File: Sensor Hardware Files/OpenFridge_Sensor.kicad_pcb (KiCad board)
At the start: 2 copper layers, 2 parts, among them U1 TMP101, U2 STM32F103C8Tx

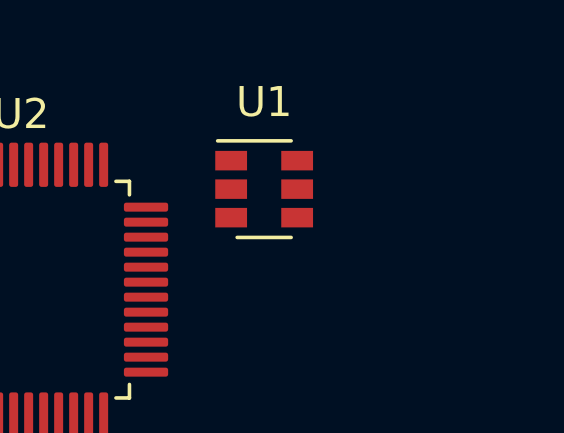
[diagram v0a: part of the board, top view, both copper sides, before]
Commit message: update bh17 footprint
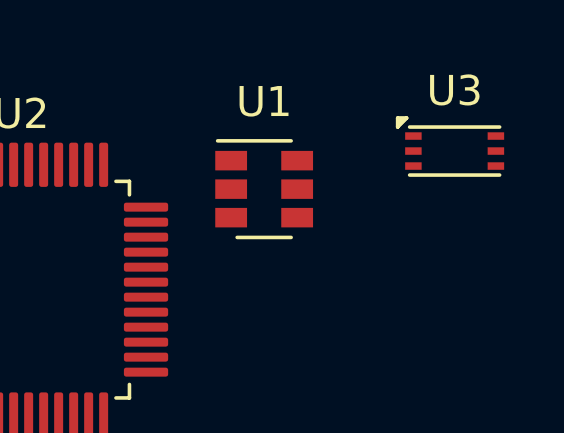
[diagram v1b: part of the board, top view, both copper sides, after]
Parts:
- added U3: BH1730FVC, OpenFridge_Sensor_Footprints:WSOF-6, F.Cu at (147.3, 86.4)

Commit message: update footprints
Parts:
- added U4: AT86RF231-ZU, Package_DFN_QFN:VQFN-32-1EP_5x5mm_P0.5mm_EP3.1x3.1mm, F.Cu at (142.2, 72.4)
- moved U3 24.7 mm to (127.0, 72.4)
- moved U1 24.4 mm to (121.9, 72.4)
- moved U2 9.26 mm to (127.0, 83.8)

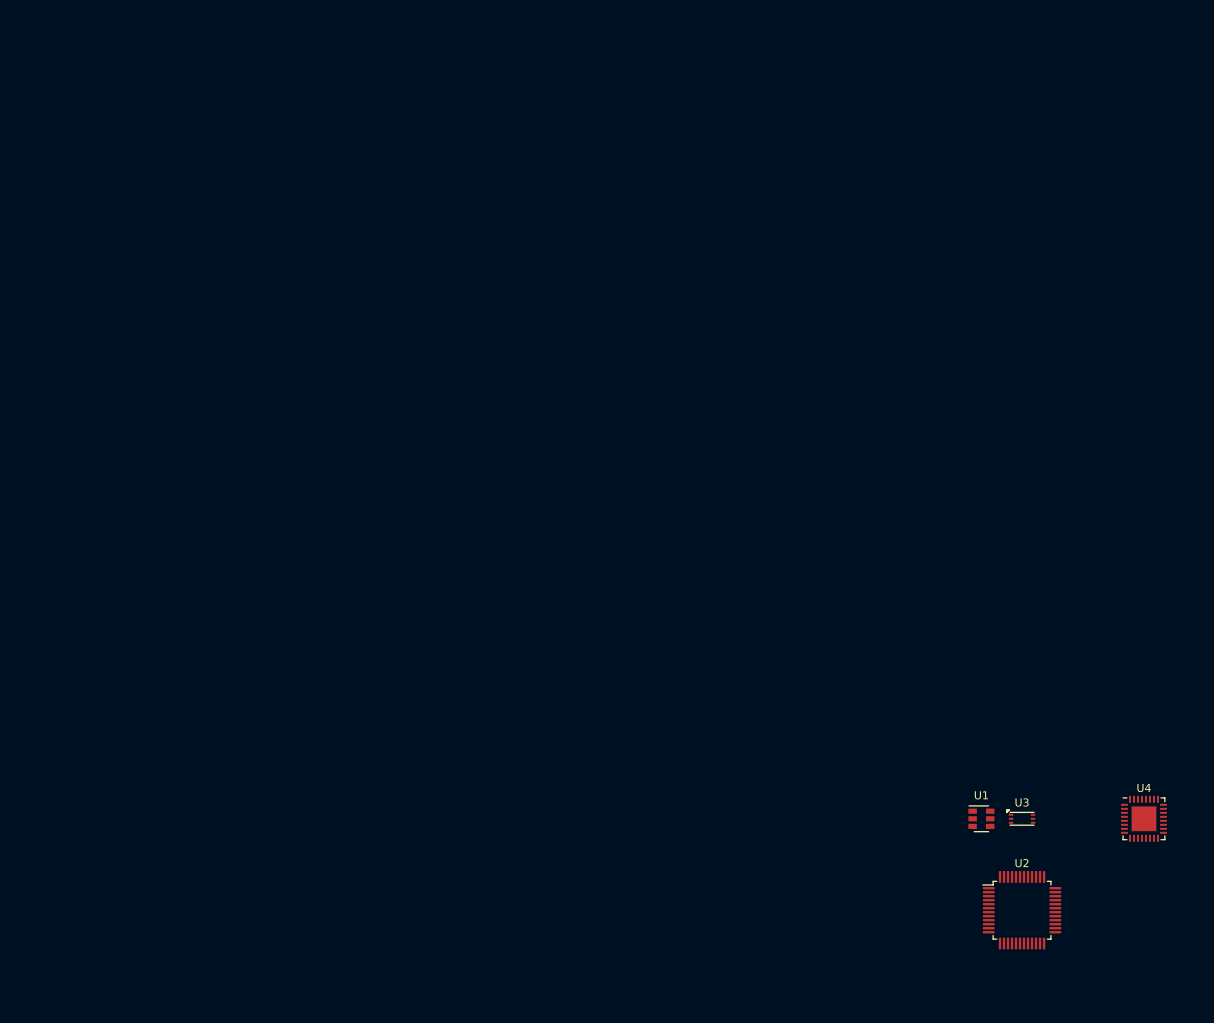
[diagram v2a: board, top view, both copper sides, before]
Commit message: add chip antenna and board outline
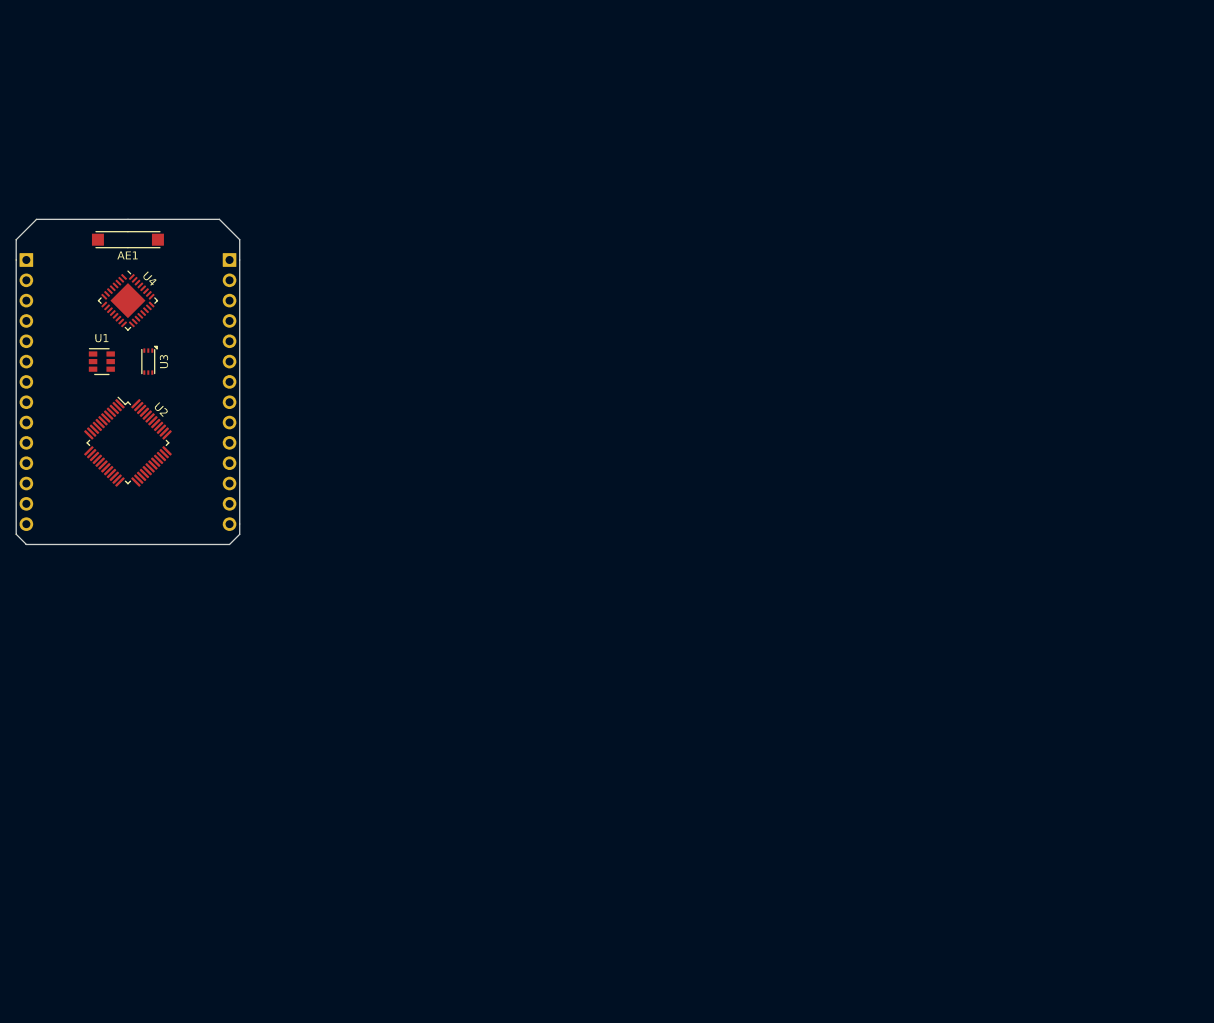
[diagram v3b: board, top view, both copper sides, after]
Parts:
- added AE1: Antenna_Chip, OpenFridge_Sensor_Footprints:RFANT8010080A3T, F.Cu at (15.2, 0.00)
- added J1: Conn_01x14, Connector_PinHeader_2.54mm:PinHeader_1x14_P2.54mm_Vertical, B.Cu at (27.9, 2.54)
- added J2: Conn_01x14, Connector_PinHeader_2.54mm:PinHeader_1x14_P2.54mm_Vertical, B.Cu at (2.54, 2.54)
- moved U4 142.6 mm to (15.2, 7.62), turned to 315 degrees
- moved U2 126.1 mm to (15.2, 25.4), turned to 315 degrees
- moved U1 123.9 mm to (12.0, 15.2)
- moved U3 123.3 mm to (17.8, 15.2), turned to 270 degrees
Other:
- board outline added: 27.9 x 40.6 mm

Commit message: update RF IC passives
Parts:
- added C1: C, Capacitor_SMD:C_0805_2012Metric_Pad1.18x1.45mm_HandSolder, F.Cu at (17.2, 6.40)
- added C2: C, Capacitor_SMD:C_0805_2012Metric_Pad1.18x1.45mm_HandSolder, F.Cu at (13.8, 5.25)
- added C3: C, Capacitor_SMD:C_0805_2012Metric_Pad1.18x1.45mm_HandSolder, F.Cu at (17.2, 4.20)
- added C4: 12pF, Capacitor_SMD:C_0805_2012Metric_Pad1.18x1.45mm_HandSolder, F.Cu at (79.6, -25.2)
- added C5: 12pF, Capacitor_SMD:C_0805_2012Metric_Pad1.18x1.45mm_HandSolder, F.Cu at (79.6, -22.2)
- added R1: R, Resistor_SMD:R_0805_2012Metric_Pad1.20x1.40mm_HandSolder, F.Cu at (11.5, 3.25)
- added Y1: 16 MHz 12pF, Crystal:Crystal_SMD_3225-4Pin_3.2x2.5mm_HandSoldering, F.Cu at (73.8, -23.9)
- U4: value AT86RF231-ZU -> XN297LBW; footprint Package_DFN_QFN:VQFN-32-1EP_5x5mm_P0.5mm_EP3.1x3.1mm -> Package_SO:SOP-8_3.9x4.9mm_P1.27mm
- moved U3 24.5 mm to (12.0, -8.60)
- moved U1 24.4 mm to (8.00, -8.80)
- moved U4 4.60 mm to (14.8, 12.2), turned to 90 degrees
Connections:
- AE1 pad 1: Net-(AE1-Pad1) -> GND
- U4 pad 7: Net-(U4-Pad7) -> GND
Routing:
- net Net-(C1-Pad2): track 0.00 -> 6.10 mm
- net Net-(C2-Pad1): track 0.00 -> 4.55 mm
- net Net-(AE1-Pad2): track 0.00 -> 2.25 mm

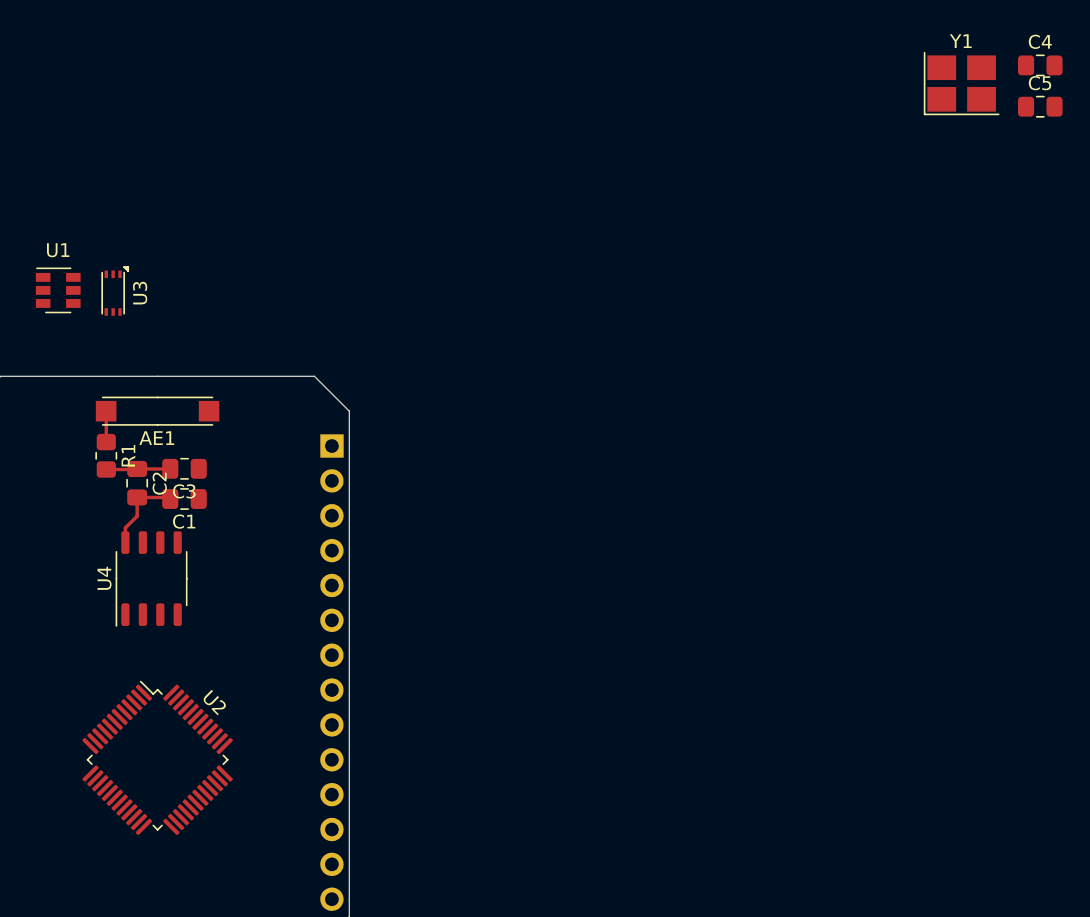
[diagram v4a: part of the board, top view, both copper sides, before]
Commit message: update rf passives
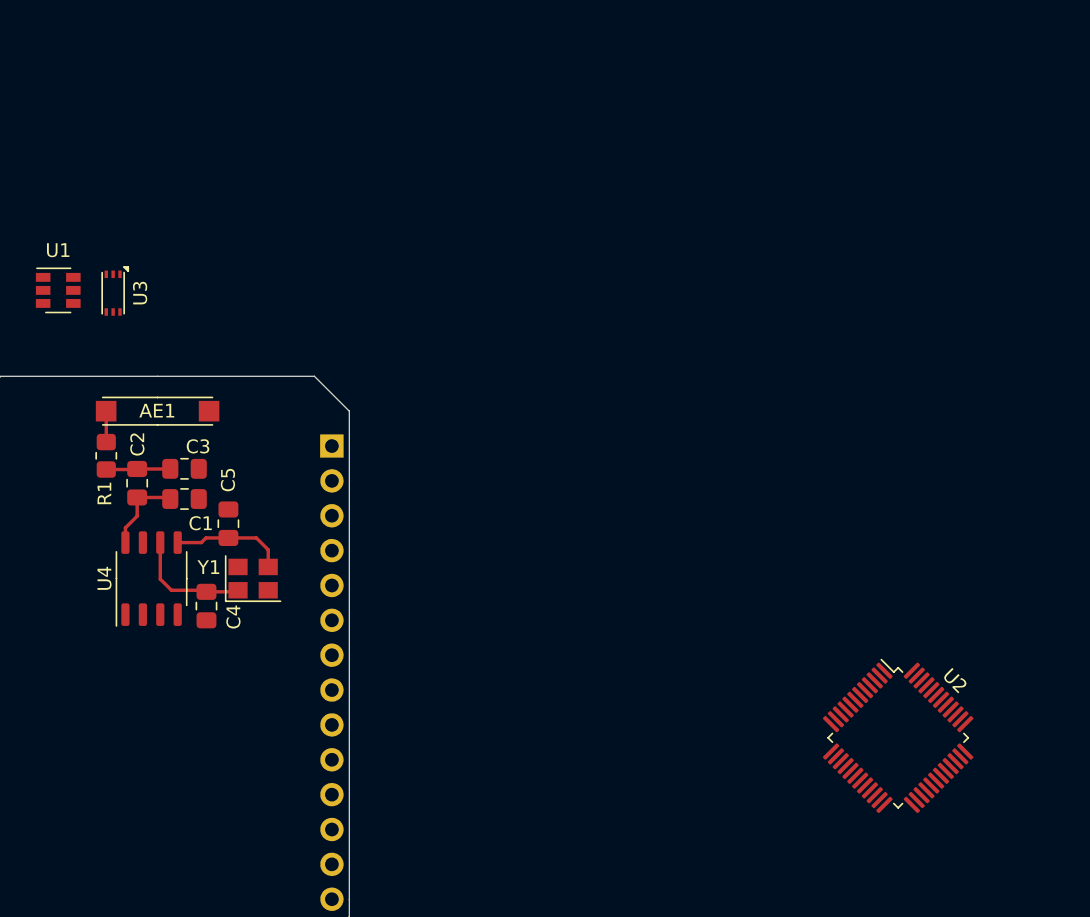
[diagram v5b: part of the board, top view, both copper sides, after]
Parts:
- Y1: footprint Crystal:Crystal_SMD_3225-4Pin_3.2x2.5mm_HandSoldering -> Crystal:Crystal_SMD_3225-4Pin_3.2x2.5mm
- moved C4 72.4 mm to (18.8, 14.2), turned to 90 degrees
- moved C5 66.5 mm to (20.4, 8.20), turned to 270 degrees
- moved Y1 63.0 mm to (22.2, 12.2)
- moved U2 54.0 mm to (69.2, 23.8)
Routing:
- net Net-(C4-Pad2): track 0.00 -> 8.81 mm
- net Net-(C5-Pad2): track 0.00 -> 8.34 mm
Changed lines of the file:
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@@
     (thickness 1.6)
     (drawings 176)
-    (tracks 11)
+    (tracks 22)
     (zones 0)
     (modules 14)
@@
     (40 Dwgs.User user)
     (41 Cmts.User user)
-    (42 Eco1.User user)
+    (42 Eco1.User user hide)
     (43 Eco2.User user)
     (44 Edge.Cuts user)
@@
     (add_net "Net-(U4-Pad4)")
   )
-  (module Crystal:Crystal_SMD_3225-4Pin_3.2x2.5mm_HandSoldering (layer F.Cu)
-    (at 73.825001 -23.874999)
-    (descr "SMD Crystal SERIES SMD3225/4 http://www.txccrystal.com/images/pdf/7m-accuracy.pdf, hand-soldering, 3.2x2.5mm^2 package")
-    (tags "SMD SMT crystal hand-soldering")
+  (module Crystal:Crystal_SMD_3225-4Pin_3.2x2.5mm (layer F.Cu)
+    (at 22.2 12.2)
+    (descr "SMD Crystal SERIES SMD3225/4 http://www.txccrystal.com/images/pdf/7m-accuracy.pdf, 3.2x2.5mm^2 package")
+    (tags "SMD SMT crystal")
     (attr smd)
-    (fp_text reference Y1 (at 0 -3.05) (layer F.SilkS)
-      (effects (font (size 1 1) (thickness 0.15)))
-    )
-    (fp_text value "16 MHz 12pF" (at 0 3.05) (layer F.Fab)
+    (fp_text reference Y1 (at -3.2 -0.8) (layer F.SilkS)
+      (effects (font (size 1 1) (thickness 0.15)))
+    )
+    (fp_text value "16 MHz 12pF" (at 0 2.45) (layer F.Fab)
       (effects (font (size 1 1) (thickness 0.15)))
     )
@@
     (fp_line (start 1.6 -1.25) (end -1.6 -1.25) (layer F.Fab) (width 0.1))
     (fp_line (start -1.6 0.25) (end -0.6 1.25) (layer F.Fab) (width 0.1))
-    (fp_line (start -2.7 -2.25) (end -2.7 2.25) (layer F.SilkS) (width 0.12))
-    (fp_line (start -2.7 2.25) (end 2.7 2.25) (layer F.SilkS) (width 0.12))
-    (fp_line (start -2.8 -2.3) (end -2.8 2.3) (layer F.CrtYd) (width 0.05))
-    (fp_line (start -2.8 2.3) (end 2.8 2.3) (layer F.CrtYd) (width 0.05))
-    (fp_line (start 2.8 2.3) (end 2.8 -2.3) (layer F.CrtYd) (width 0.05))
-    (fp_line (start 2.8 -2.3) (end -2.8 -2.3) (layer F.CrtYd) (width 0.05))
-    (pad 4 smd rect (at -1.45 -1.15) (size 2.1 1.8) (layers F.Cu F.Paste F.Mask)
+    (fp_line (start -2 -1.65) (end -2 1.65) (layer F.SilkS) (width 0.12))
+    (fp_line (start -2 1.65) (end 2 1.65) (layer F.SilkS) (width 0.12))
+    (fp_line (start -2.1 -1.7) (end -2.1 1.7) (layer F.CrtYd) (width 0.05))
+    (fp_line (start -2.1 1.7) (end 2.1 1.7) (layer F.CrtYd) (width 0.05))
+    (fp_line (start 2.1 1.7) (end 2.1 -1.7) (layer F.CrtYd) (width 0.05))
+    (fp_line (start 2.1 -1.7) (end -2.1 -1.7) (layer F.CrtYd) (width 0.05))
+    (pad 4 smd rect (at -1.1 -0.85) (size 1.4 1.2) (layers F.Cu F.Paste F.Mask)
       (net 92 GND))
-    (pad 3 smd rect (at 1.45 -1.15) (size 2.1 1.8) (layers F.Cu F.Paste F.Mask)
+    (pad 3 smd rect (at 1.1 -0.85) (size 1.4 1.2) (layers F.Cu F.Paste F.Mask)
       (net 96 "Net-(C5-Pad2)"))
-    (pad 2 smd rect (at 1.45 1.15) (size 2.1 1.8) (layers F.Cu F.Paste F.Mask)
+    (pad 2 smd rect (at 1.1 0.85) (size 1.4 1.2) (layers F.Cu F.Paste F.Mask)
       (net 92 GND))
-    (pad 1 smd rect (at -1.45 1.15) (size 2.1 1.8) (layers F.Cu F.Paste F.Mask)
+    (pad 1 smd rect (at -1.1 0.85) (size 1.4 1.2) (layers F.Cu F.Paste F.Mask)
       (net 95 "Net-(C4-Pad2)"))
-    (model ${KISYS3DMOD}/Crystal.3dshapes/Crystal_SMD_3225-4Pin_3.2x2.5mm_HandSoldering.wrl
+    (model ${KISYS3DMOD}/Crystal.3dshapes/Crystal_SMD_3225-4Pin_3.2x2.5mm.wrl
       (at (xyz 0 0 0))
       (scale (xyz 1 1 1))
@@
   )
   (module Capacitor_SMD:C_0805_2012Metric_Pad1.18x1.45mm_HandSolder (layer F.Cu)
-    (at 79.555001 -22.184999)
+    (at 20.4 8.2 270)
     (descr "Capacitor SMD 0805 (2012 Metric), square (rectangular) end terminal, IPC_7351 nominal with elongated pad for handsoldering. (Body size source: IPC-SM-782 page 76, https://www.pcb-3d.com/wordpress/wp-content/uploads/ipc-sm-782a_amendment_1_and_2.pdf, https://docs.google.com/spreadsheets/d/1BsfQQcO9C6DZCsRaXUlFlo91Tg2WpOkGARC1WS5S8t0/edit?usp=sharing), generated with kicad-footprint-generator")
     (tags "capacitor handsolder")
     (attr smd)
-    (fp_text reference C5 (at 0 -1.68) (layer F.SilkS)
-      (effects (font (size 1 1) (thickness 0.15)))
-    )
-    (fp_text value 12pF (at 0 1.68) (layer F.Fab)
-      (effects (font (size 1 1) (thickness 0.15)))
-    )
-    (fp_text user %R (at 0 0) (layer F.Fab)
+    (fp_text reference C5 (at -3.2 0 90) (layer F.SilkS)
+      (effects (font (size 1 1) (thickness 0.15)))
+    )
+    (fp_text value 12pF (at 0 1.68 90) (layer F.Fab)
+      (effects (font (size 1 1) (thickness 0.15)))
+    )
+    (fp_text user %R (at 0 0 90) (layer F.Fab)
       (effects (font (size 0.5 0.5) (thickness 0.08)))
     )
@@
     (fp_line (start 1.88 -0.98) (end 1.88 0.98) (layer F.CrtYd) (width 0.05))
     (fp_line (start 1.88 0.98) (end -1.88 0.98) (layer F.CrtYd) (width 0.05))
-    (pad 2 smd roundrect (at 1.0375 0) (size 1.175 1.45) (layers F.Cu F.Paste F.Mask) (roundrect_rratio 0.212766)
+    (pad 2 smd roundrect (at 1.0375 0 270) (size 1.175 1.45) (layers F.Cu F.Paste F.Mask) (roundrect_rratio 0.212766)
       (net 96 "Net-(C5-Pad2)"))
-    (pad 1 smd roundrect (at -1.0375 0) (size 1.175 1.45) (layers F.Cu F.Paste F.Mask) (roundrect_rratio 0.212766)
+    (pad 1 smd roundrect (at -1.0375 0 270) (size 1.175 1.45) (layers F.Cu F.Paste F.Mask) (roundrect_rratio 0.212766)
       (net 92 GND))
     (model ${KISYS3DMOD}/Capacitor_SMD.3dshapes/C_0805_2012Metric.wrl
@@
   )
   (module Capacitor_SMD:C_0805_2012Metric_Pad1.18x1.45mm_HandSolder (layer F.Cu)
-    (at 79.555001 -25.194999)
+    (at 18.8 14.2 90)
     (descr "Capacitor SMD 0805 (2012 Metric), square (rectangular) end terminal, IPC_7351 nominal with elongated pad for handsoldering. (Body size source: IPC-SM-782 page 76, https://www.pcb-3d.com/wordpress/wp-content/uploads/ipc-sm-782a_amendment_1_and_2.pdf, https://docs.google.com/spreadsheets/d/1BsfQQcO9C6DZCsRaXUlFlo91Tg2WpOkGARC1WS5S8t0/edit?usp=sharing), generated with kicad-footprint-generator")
     (tags "capacitor handsolder")
     (attr smd)
-    (fp_text reference C4 (at 0 -1.68) (layer F.SilkS)
-      (effects (font (size 1 1) (thickness 0.15)))
-    )
-    (fp_text value 12pF (at 0 1.68) (layer F.Fab)
-      (effects (font (size 1 1) (thickness 0.15)))
-    )
-    (fp_text user %R (at 0 0) (layer F.Fab)
+    (fp_text reference C4 (at -0.8 2 90) (layer F.SilkS)
+      (effects (font (size 1 1) (thickness 0.15)))
+    )
+    (fp_text value 12pF (at 0 1.68 90) (layer F.Fab)
+      (effects (font (size 1 1) (thickness 0.15)))
+    )
+    (fp_text user %R (at 0 0 90) (layer F.Fab)
       (effects (font (size 0.5 0.5) (thickness 0.08)))
     )
@@
     (fp_line (start 1.88 -0.98) (end 1.88 0.98) (layer F.CrtYd) (width 0.05))
     (fp_line (start 1.88 0.98) (end -1.88 0.98) (layer F.CrtYd) (width 0.05))
-    (pad 2 smd roundrect (at 1.0375 0) (size 1.175 1.45) (layers F.Cu F.Paste F.Mask) (roundrect_rratio 0.212766)
+    (pad 2 smd roundrect (at 1.0375 0 90) (size 1.175 1.45) (layers F.Cu F.Paste F.Mask) (roundrect_rratio 0.212766)
       (net 95 "Net-(C4-Pad2)"))
-    (pad 1 smd roundrect (at -1.0375 0) (size 1.175 1.45) (layers F.Cu F.Paste F.Mask) (roundrect_rratio 0.212766)
+    (pad 1 smd roundrect (at -1.0375 0 90) (size 1.175 1.45) (layers F.Cu F.Paste F.Mask) (roundrect_rratio 0.212766)
       (net 92 GND))
     (model ${KISYS3DMOD}/Capacitor_SMD.3dshapes/C_0805_2012Metric.wrl
@@
     (tags "resistor handsolder")
     (attr smd)
-    (fp_text reference R1 (at 0 -1.65 90) (layer F.SilkS)
+    (fp_text reference R1 (at 2.75 0.1 90) (layer F.SilkS)
       (effects (font (size 1 1) (thickness 0.15)))
     )
@@
     (tags "capacitor handsolder")
     (attr smd)
-    (fp_text reference C3 (at 0 -1.68) (layer F.SilkS)
+    (fp_text reference C3 (at -1 1.6) (layer F.SilkS)
       (effects (font (size 1 1) (thickness 0.15)))
     )
@@
     (tags "capacitor handsolder")
     (attr smd)
-    (fp_text reference C2 (at 0 -1.68 90) (layer F.SilkS)
+    (fp_text reference C2 (at -2.85 -0.05 90) (layer F.SilkS)
       (effects (font (size 1 1) (thickness 0.15)))
     )
@@
     (tags "capacitor handsolder")
     (attr smd)
-    (fp_text reference C1 (at 0 -1.68) (layer F.SilkS)
+    (fp_text reference C1 (at -1.2 -1.8) (layer F.SilkS)
       (effects (font (size 1 1) (thickness 0.15)))
     )
@@
   (module OpenFridge_Sensor_Footprints:RFANT8010080A3T (layer F.Cu)
     (at 15.24 0 180)
-    (fp_text reference AE1 (at 0 -2) (layer F.SilkS)
+    (fp_text reference AE1 (at 0 0) (layer F.SilkS)
       (effects (font (size 1 1) (thickness 0.15)))
     )
@@
   )
   (module Package_QFP:LQFP-48_7x7mm_P0.5mm (layer F.Cu)
-    (at 15.24 25.4 315)
+    (at 69.2 23.8 315)
     (descr "LQFP, 48 Pin (https://www.analog.com/media/en/technical-documentation/data-sheets/ltc2358-16.pdf), generated with kicad-footprint-generator ipc_gullwing_generator.py")
     (tags "LQFP QFP")
@@
   (segment (start 15.925 4.2125) (end 16 4.2875) (width 0.25) (layer F.Cu) (net 94))
   (segment (start 13.75 4.2125) (end 15.925 4.2125) (width 0.25) (layer F.Cu) (net 94))
+  (segment (start 18.9 13.05) (end 16.25 13.05) (width 0.25) (layer F.Cu) (net 95))
+  (segment (start 15.435 12.235) (end 15.435 9.575) (width 0.25) (layer F.Cu) (net 95))
+  (segment (start 16.25 13.05) (end 15.435 12.235) (width 0.25) (layer F.Cu) (net 95))
+  (segment (start 20.9875 13.1625) (end 21.1 13.05) (width 0.25) (layer F.Cu) (net 95))
+  (segment (start 18.8 13.1625) (end 20.9875 13.1625) (width 0.25) (layer F.Cu) (net 95))
+  (segment (start 16.705 9.575) (end 18.425 9.575) (width 0.25) (layer F.Cu) (net 96))
+  (segment (start 18.7625 9.2375) (end 20.4 9.2375) (width 0.25) (layer F.Cu) (net 96))
+  (segment (start 18.425 9.575) (end 18.7625 9.2375) (width 0.25) (layer F.Cu) (net 96))
+  (segment (start 23.3 10.1) (end 23.3 11.35) (width 0.25) (layer F.Cu) (net 96))
+  (segment (start 22.4375 9.2375) (end 23.3 10.1) (width 0.25) (layer F.Cu) (net 96))
+  (segment (start 20.4 9.2375) (end 22.4375 9.2375) (width 0.25) (layer F.Cu) (net 96))
 )
